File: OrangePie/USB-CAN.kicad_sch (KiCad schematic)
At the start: 0 parts

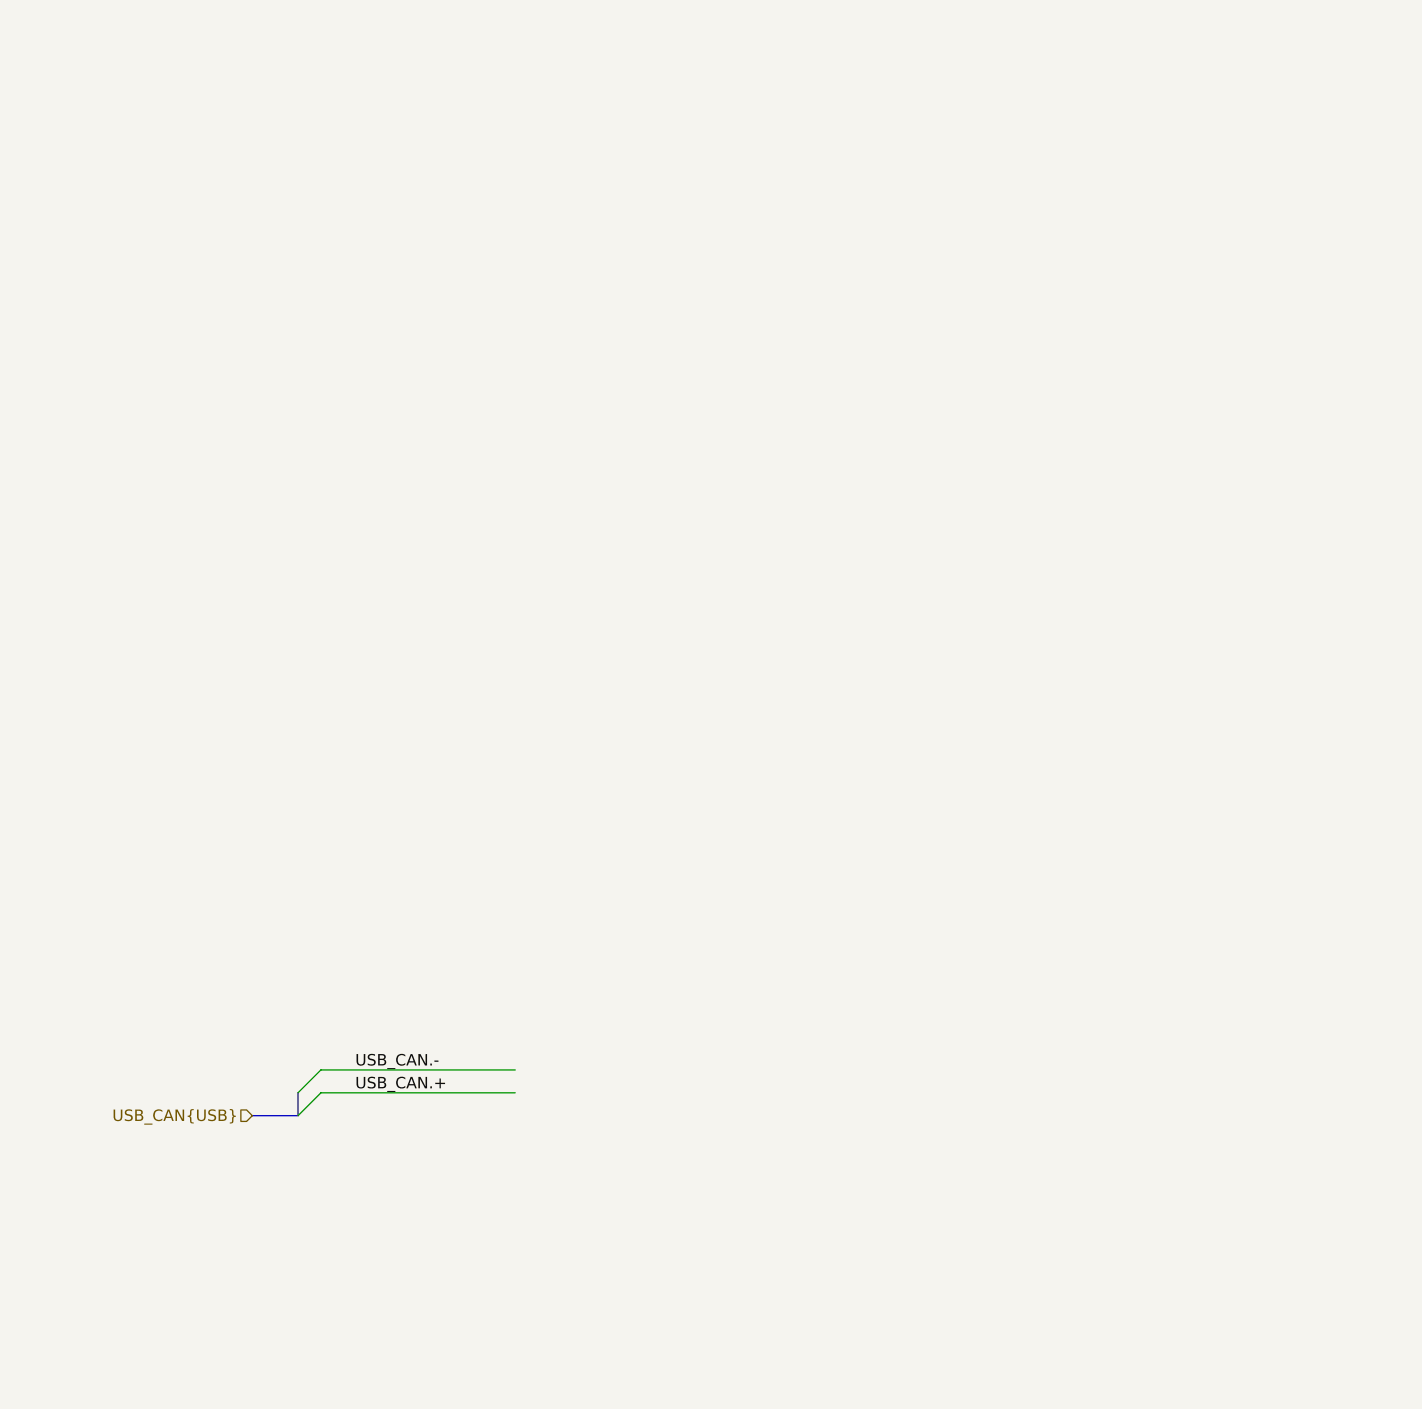
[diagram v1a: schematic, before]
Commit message: Update rest of schematic
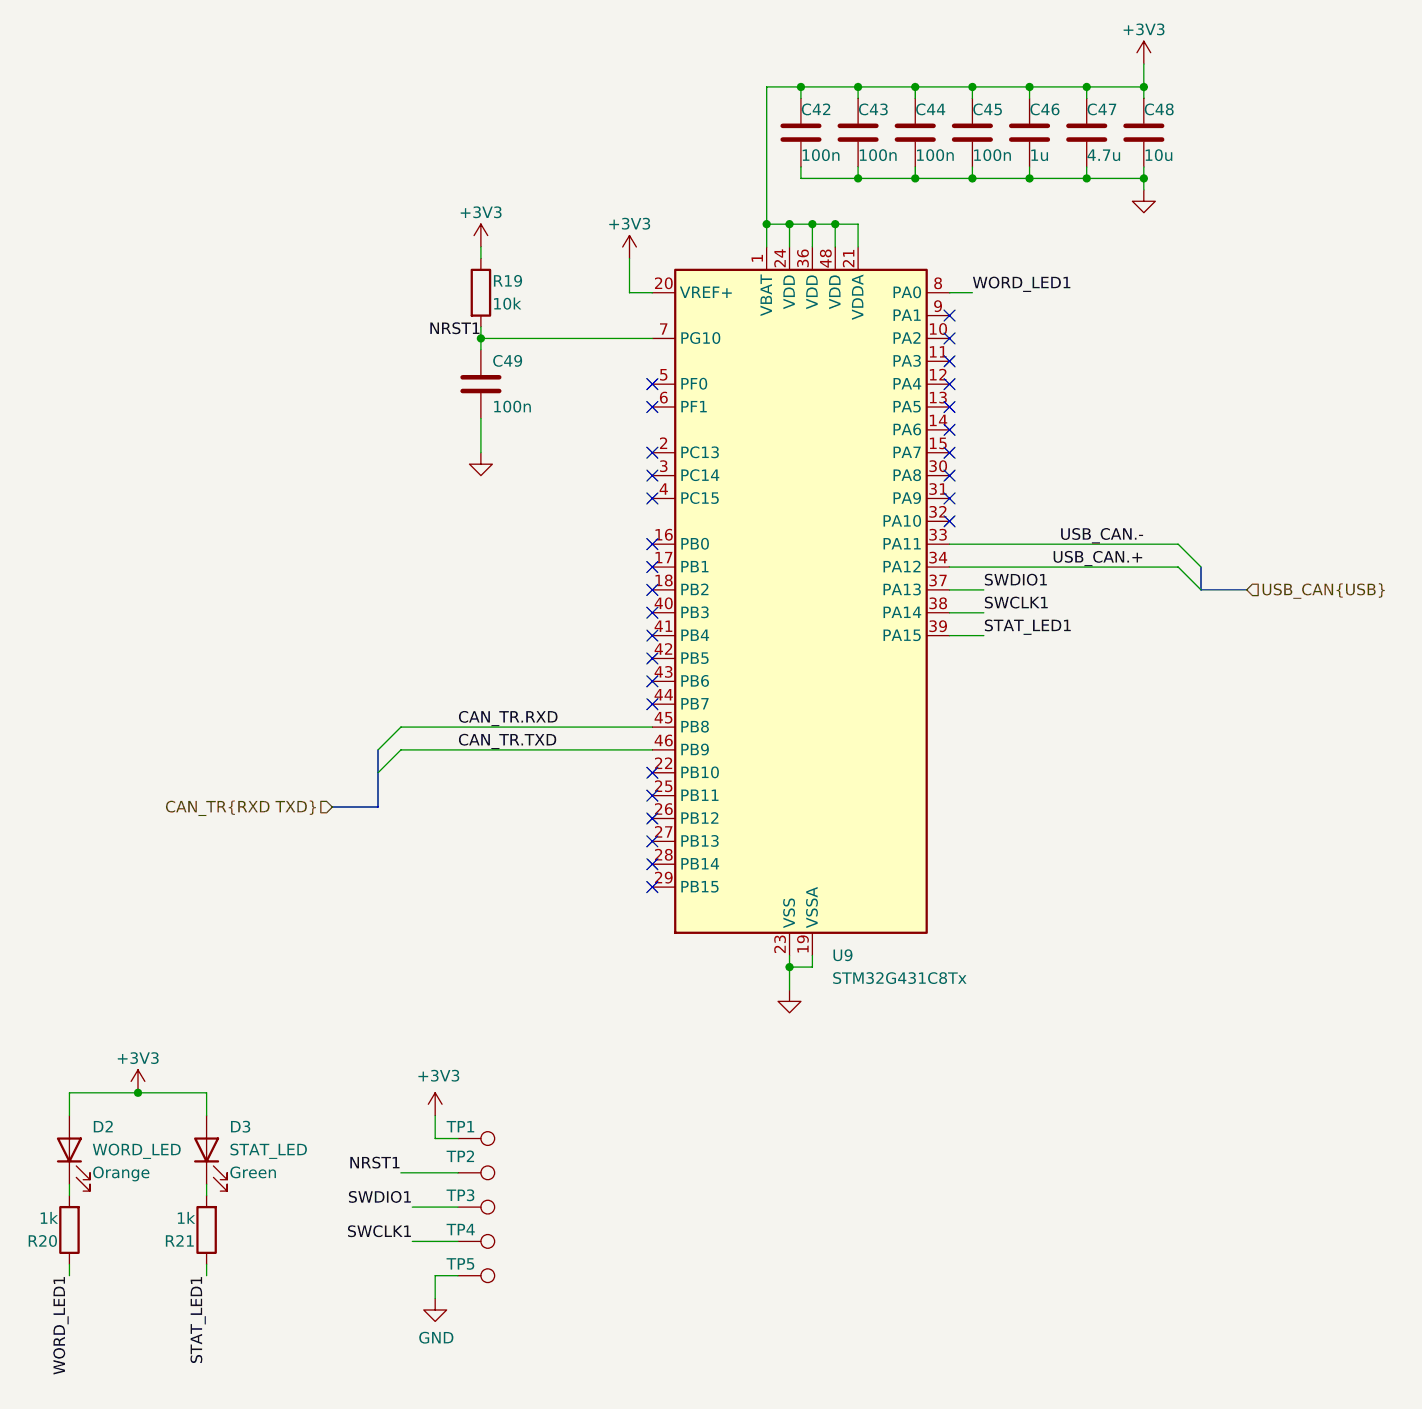
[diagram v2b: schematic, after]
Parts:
- added C42, C43, C44, C45, C49: 100n, Capacitor_SMD:C_0402_1005Metric, symbol Device:C
- added C46: 1u, Capacitor_SMD:C_0603_1608Metric, symbol Device:C
- added C47: 4.7u, Capacitor_SMD:C_0603_1608Metric, symbol Device:C
- added C48: 10u, Capacitor_SMD:C_0805_2012Metric, symbol Device:C
- added D2: WORD_LED, Diode_SMD:D_0603_1608Metric, symbol Device:LED
- added D3: STAT_LED, Diode_SMD:D_0603_1608Metric, symbol Device:LED
- added R19: 10k, Resistor_SMD:R_0402_1005Metric, symbol Device:R
- added R20, R21: 1k, Resistor_SMD:R_0402_1005Metric, symbol Device:R
- added TP1, TP2, TP3, TP4, TP5: ~, TestPoint:TestPoint_Pad_1.0x1.0mm, symbol Connector:TestPoint
- added U9: STM32G431C8Tx, Package_QFP:LQFP-48_7x7mm_P0.5mm, symbol MCU_ST_STM32G4:STM32G431C8Tx
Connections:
- net USB_CAN.+: now also U9.34 (PA12)
- net USB_CAN.-: now also U9.33 (PA11)
- new net: D3.1 (K), R21.2
- new net: D2.1 (K), R20.2
- new net +3V3: C42.1, C43.1, C44.1, C45.1, C46.1, C47.1, C48.1, D2.2 (A), D3.2 (A), R19.1, TP1.1, U9.1 (VBAT), U9.20 (VREF+), U9.21 (VDDA), U9.24 (VDD), U9.36 (VDD), U9.48 (VDD)
- new net CAN_TR.RXD: U9.45 (PB8)
- new net CAN_TR.TXD: U9.46 (PB9)
- new net GND: C42.2, C43.2, C44.2, C45.2, C46.2, C47.2, C48.2, C49.2, TP5.1, U9.19 (VSSA), U9.23 (VSS), U9.35 (VSS), U9.47 (VSS)
- new net NRST1: C49.1, R19.2, TP2.1, U9.7 (PG10)
- new net STAT_LED1: R21.1, U9.39 (PA15)
- new net SWCLK1: TP4.1, U9.38 (PA14)
- new net SWDIO1: TP3.1, U9.37 (PA13)
- new net WORD_LED1: R20.1, U9.8 (PA0)
- no-connect marks 0 -> 29

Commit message: Add CH340 debug
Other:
- company: (none) -> ModuCard System
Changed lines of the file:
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@@
 	(generator_version "8.0")
 	(paper "A4")
+	(title_block
+		(date "2025-02-10")
+		(rev "A")
+		(company "ModuCard System")
+	)
 	(junction
 		(at 140.97 135.89)
